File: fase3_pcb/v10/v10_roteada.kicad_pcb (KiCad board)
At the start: 6 copper layers, 190 x 145 mm, 319 parts, among them J1 AMASS, J2 USB, Q1 TO-252-2, SW1 SW, SW2 SW, U10 SOIC-16, U11 SOIC-16, U8 SOIC-16, U9 SOIC-16

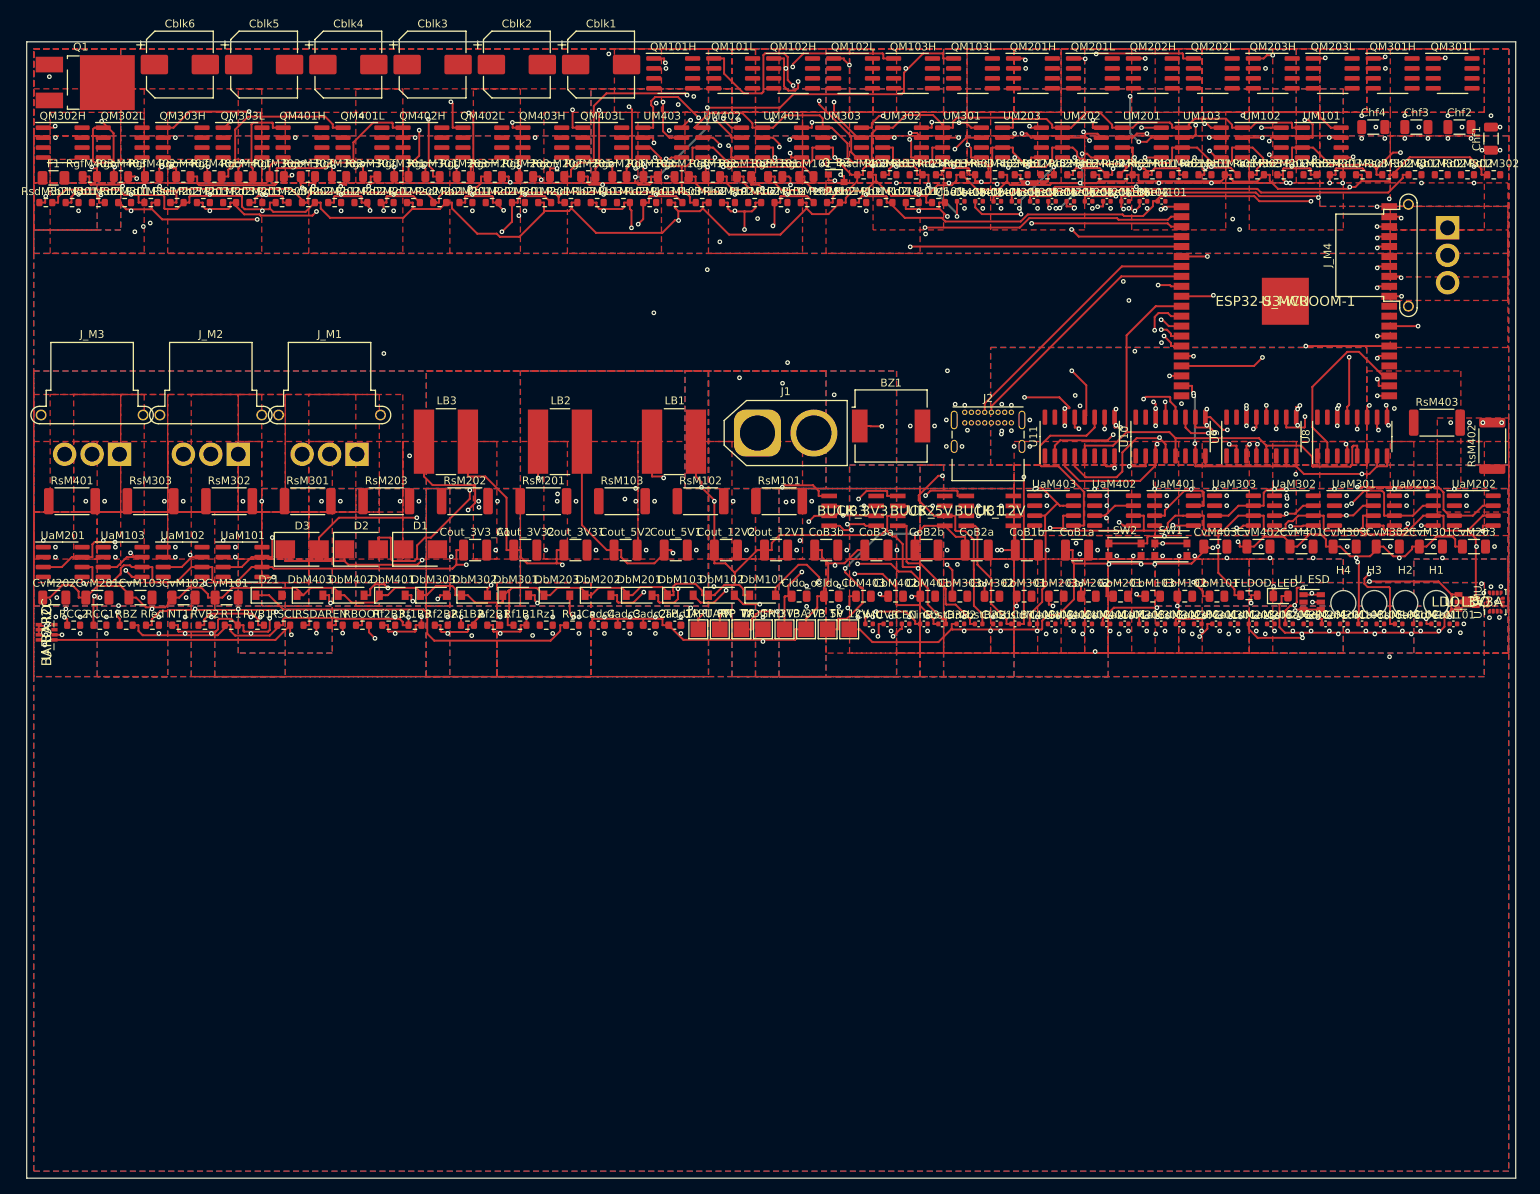
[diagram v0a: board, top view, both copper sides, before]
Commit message: feat(v10): placa FABRICAVEL — re-roteada com keepouts, G1-G8 TODO OK, SES via SesFromFrb
Fechamento do re-roteamento com os 3.167 keepouts de cobre excluido:

- Board roteado NOVO (v10_roteada): TODOS OS GATES OK (G1-G8) — primeira
  vez. Antes: G6=16 pads sem via, G8=354 curtos trilha x cobre-excluido.
  Agora: G6=0, G8=0. A placa esta' LIVRE DE CURTOS — fabricavel.
- SES extraido do estado bancado de 5 passadas (3,6 h de roteamento,
  .frb 846 KB) pelo utilitario NOVO freerouting/SesFromFrb.java: carrega
  o RoutingBoard serializado do .frb e grava o SES direto
  (ObjectInputStream -> RoutingBoard -> SpecctraSesFileWriter.write)
  — sem GUI e sem esperar a convergencia do batch (com keepouts cada
  passada custa ~44 min vs ~6 min antes).
- Numeros: 1.208 wires, 374 vias de rota no SES; 3.499 trilhas + 823
  vias (449 stitch + 374 rota) no board; 133/151 nets (18 air-wires
  documentados no ERROS_CONHECIDOS 9.6 — ausencias, nao curtos).
- Verificacao_v10.txt = board ROTEADO (o entregavel) — base segue verde
  no relatorio do harness [B].
- Logs completos do run (full3 + resume + watchdog + interno) commitados.
- ERROS_CONHECIDOS 9.6: tabela antes/depois + opcoes para as 18 nets.

Harness agora reprova SO no que falta de verdade: as 18 air-wires e o
preco do MCP3208 (sessao de navegador do usuario).
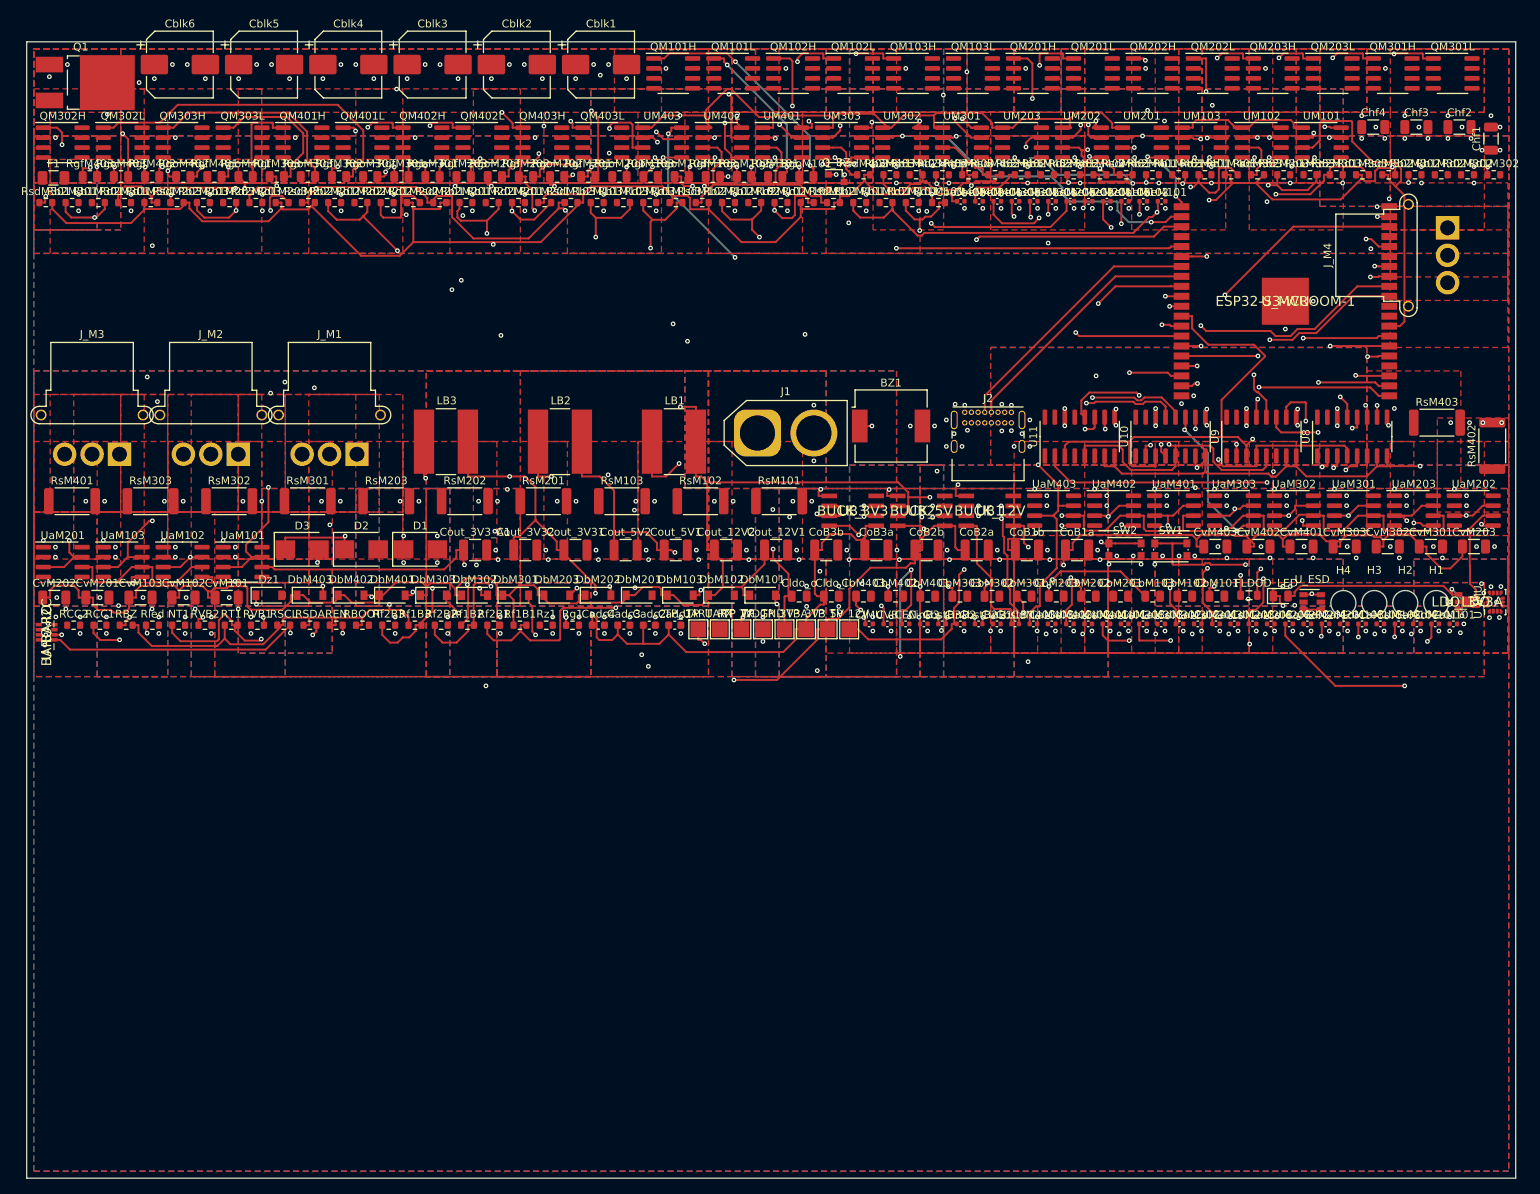
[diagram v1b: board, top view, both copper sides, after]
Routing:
- net I_M201: track 169.0 -> 0.00 mm, vias 2 -> 0
- net I_M101: track 155.0 -> 0.00 mm, vias 2 -> 0
- net VBUS_USB: track 152.6 -> 0.00 mm, vias 3 -> 0
- net UART_TX: track 135.2 -> 0.00 mm, vias 3 -> 0
- net CC2: track 131.9 -> 0.00 mm, vias 1 -> 0
- net VBM201: track 130.1 -> 0.00 mm, vias 3 -> 0
- net VBM102: track 127.2 -> 0.00 mm, vias 3 -> 0
- net BOOT_N: track 173.7 -> 59.3 mm, vias 5 -> 2
- net 3V3_IMU: track 166.4 -> 73.5 mm, vias 3 -> 2
- net HOM303: track 85.4 -> 0.00 mm, vias 4 -> 0
- net HOM201: track 83.1 -> 0.00 mm, vias 4 -> 0
- net LOM101: track 80.5 -> 0.00 mm, vias 2 -> 0
- net LOM401: track 80.1 -> 0.00 mm, vias 2 -> 0
- net HOM302: track 77.5 -> 0.00 mm, vias 2 -> 0
- net VBM103: track 126.3 -> 60.9 mm, vias 3 -> 2
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
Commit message: feat(v10): cobertura 134/151 — completude de roteamento + multi-SES + BOM + README
Erros restantes resolvidos (pedido do usuario, 12/10):

- COMPLETUDE DE ROTEAMENTO: dsn_export.py agora exporta as trilhas/vias de
  sinal existentes como (wiring ...) com (type fix) — o FR as trata como
  pre-rotas intocaveis (SYSTEM_FIXED) e rotea SO o que falta ao redor delas.
  Rodada de completude (31min38s autorrotear + 23min59s otimizar) fechou a
  PWM_M203. Cobertura: 133/151 -> 134/151. As 17 restantes sao o nucleo
  congestionado (I_M/HOM/LOM/VBM/IMU) — ganho marginal do FR e' ~1 net/30min;
  recomendado roteamento manual ou revisao v11 do layout.
- ses_import.py: aceita multiplos SESes (pcb_in ses1 ses2... pcb_out) com
  DEDUPLICACAO exata (635 segmentos re-exportados pelo SES de completude
  foram pulados em vez de duplicados).
- Board v10_roteada mesclado e VERIFICADO: TODOS OS GATES G1-G8 OK (G8=0,
  as rotas novas respeitaram os keepouts). verificacao_v10.txt = roteado.
- BOM: preco do MCP3208 preenchido com a referencia documentada do proprio
  ORCAMENTO.md §6 (US$ 2,60, LCSC C626764, RECOTAR NA COMPRA); estoque do
  ADS7953 errado removido. Harness [E]: ZERO linhas compraveis sem preco.
- README.md: reescrito para o estado real de 12/10 (board roteado G1-G8,
  pipeline com keepouts, harness, estrutura e comandos de reproducao).
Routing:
- net 3V3: track 631.8 -> 984.8 mm, vias 17 -> 19
- net 12V: track 465.1 -> 771.4 mm, vias 6 -> 7
- net VREFM201: track 229.2 -> 458.4 mm
- net I2C_SCL: track 209.9 -> 418.5 mm
- net VBAT_SENSE: track 205.8 -> 405.6 mm
- net I2C_SDA: track 200.7 -> 399.8 mm
- net VREFM301: track 218.4 -> 415.7 mm
- net I_M103: track 189.3 -> 374.4 mm
- net SD_MCU: track 221.9 -> 393.8 mm
- net VREFM101: track 226.8 -> 397.1 mm
- net TEMP_SENSE: track 199.6 -> 359.5 mm
- net RB_M301: track 172.3 -> 319.0 mm
- net CC1: track 143.7 -> 287.6 mm
- net I_M102: track 176.1 -> 318.1 mm
- net VBM403: track 146.0 -> 283.3 mm, vias 6 -> 7
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
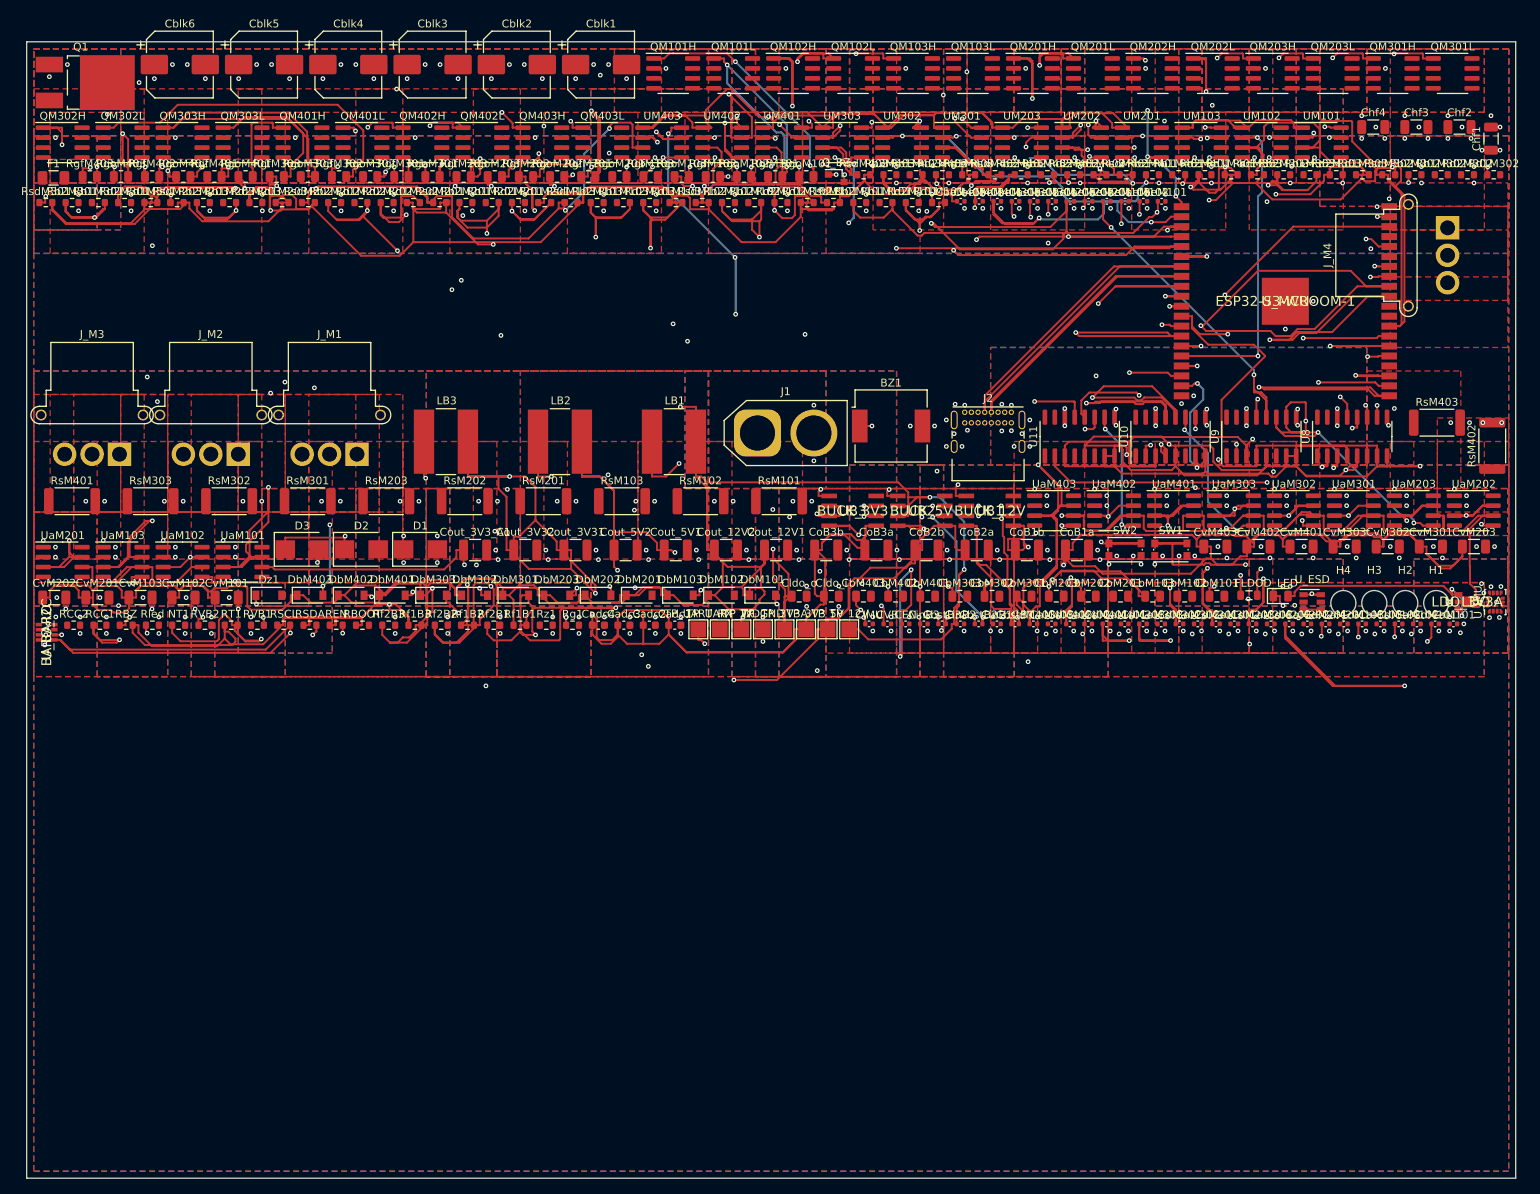
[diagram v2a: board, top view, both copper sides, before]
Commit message: docs(v10): README no estado real + rodada 2 de completude (134/151, G1-G8 OK)
- README.md: status preciso — 134/151 nets de sinal roteadas, as 17
  air-wires listadas (nucleo congestionado de potencia), recomendacao
  (manual no KiCad ou revisao v11 do layout) e pipeline/documentacao
  completos.
- Rodada 2 de completude (28min10s rotear + 27min25s otimizar): poliu
  as rotas mas nao fechou nova net — as 17 sao o limite real do batch.
  Artifacts: v10_completion2.dsn/ses + completion3_run.log.
- Board v10_roteada (3 SESes mesclados, 6133 trilhas + 847 vias,
  2200 duplicatas puladas): TODOS OS GATES G1-G8 OK (verificacao_v10.txt).
- verificacoes/verifica_projeto.py: [A] agora conta a UNIAO de todos os
  SESes do run (v10_final + v10_completion*) — coerente com o pipeline
  multi-SES.
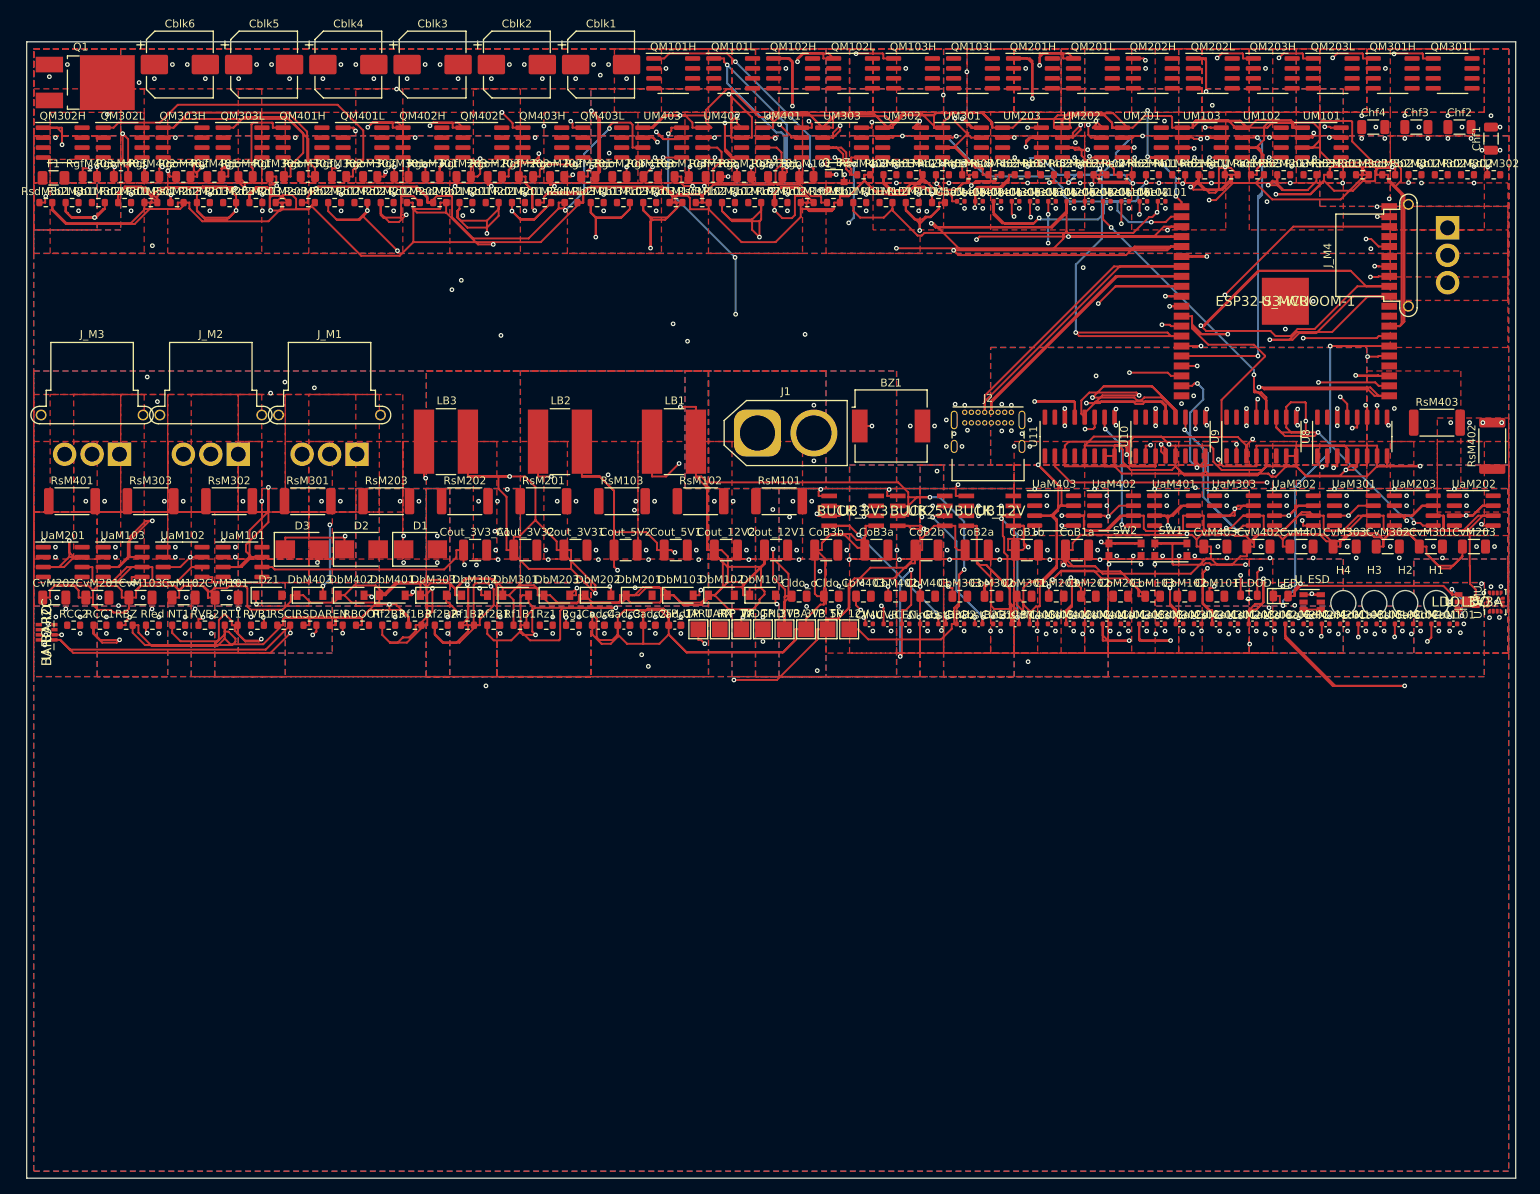
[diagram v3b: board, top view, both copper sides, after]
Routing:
- net RB_M301: track 319.0 -> 487.2 mm
- net 12V: track 771.4 -> 934.5 mm
- net 3V3: track 984.8 -> 1141.7 mm, vias 19 -> 21
- net VREFM301: track 415.7 -> 558.8 mm
- net VBM301: track 159.4 -> 300.2 mm
- net RB_M202: track 194.3 -> 327.3 mm, vias 5 -> 6
- net VBM303: track 214.0 -> 342.6 mm
- net VBM302: track 269.7 -> 393.1 mm
- net VBM103: track 149.1 -> 268.5 mm
- net GHM301: track 249.4 -> 368.6 mm
- net VBM401: track 269.1 -> 388.2 mm
- net RB_M203: track 238.6 -> 355.1 mm
- net RB_M201: track 178.3 -> 291.9 mm
- net CC1: track 287.6 -> 394.2 mm
- net VBM402: track 243.1 -> 344.4 mm
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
